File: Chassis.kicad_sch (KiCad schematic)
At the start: 26 parts, among them J1 FR_JST, J10 BL_XT30, J11 Sabre Vertical Header 6, J2 FR_XT30, J3 BR_JST, J4 BR_XT30, J5 IN_JST, J6 IN_XT60, J7 FL_JST, J8 FL_XT30, J9 BL_JST

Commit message: updated xt30 footprints
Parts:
- J10, J2, J4, J8: footprint Robomaster_ICs:AMASS_XT30U-F_1x02_P5.0mm_Vertical -> Connector_AMASS:AMASS_XT30UPB-F_1x02_P5.0mm_Vertical
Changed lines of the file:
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@@
       (effects (font (size 1.27 1.27)))
     )
-    (property "Footprint" "Robomaster_ICs:AMASS_XT30U-F_1x02_P5.0mm_Vertical" (at 130.81 96.52 0)
+    (property "Footprint" "Connector_AMASS:AMASS_XT30UPB-F_1x02_P5.0mm_Vertical" (at 130.81 96.52 0)
       (effects (font (size 1.27 1.27)) hide)
     )
@@
       (effects (font (size 1.27 1.27)))
     )
-    (property "Footprint" "Robomaster_ICs:AMASS_XT30U-F_1x02_P5.0mm_Vertical" (at 130.81 121.92 0)
+    (property "Footprint" "Connector_AMASS:AMASS_XT30UPB-F_1x02_P5.0mm_Vertical" (at 130.81 121.92 0)
       (effects (font (size 1.27 1.27)) hide)
     )
@@
       (effects (font (size 1.27 1.27)))
     )
-    (property "Footprint" "Robomaster_ICs:AMASS_XT30U-F_1x02_P5.0mm_Vertical" (at 130.81 147.32 0)
+    (property "Footprint" "Connector_AMASS:AMASS_XT30UPB-F_1x02_P5.0mm_Vertical" (at 130.81 147.32 0)
       (effects (font (size 1.27 1.27)) hide)
     )
@@
       (effects (font (size 1.27 1.27)))
     )
-    (property "Footprint" "Robomaster_ICs:AMASS_XT30U-F_1x02_P5.0mm_Vertical" (at 130.81 69.85 0)
-      (effects (font (size 1.27 1.27)) hide)
-    )
+    (property "Footprint" "Connector_AMASS:AMASS_XT30UPB-F_1x02_P5.0mm_Vertical" (at 130.81 69.85 0)
+      (effects (font (size 1.27 1.27)) hide)
+    )

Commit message: Add box to schematic
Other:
- note added: "Mounting Holes"
- moved on the sheet: H1, H2, H3, H4, H5, H6, H7, H8, H9

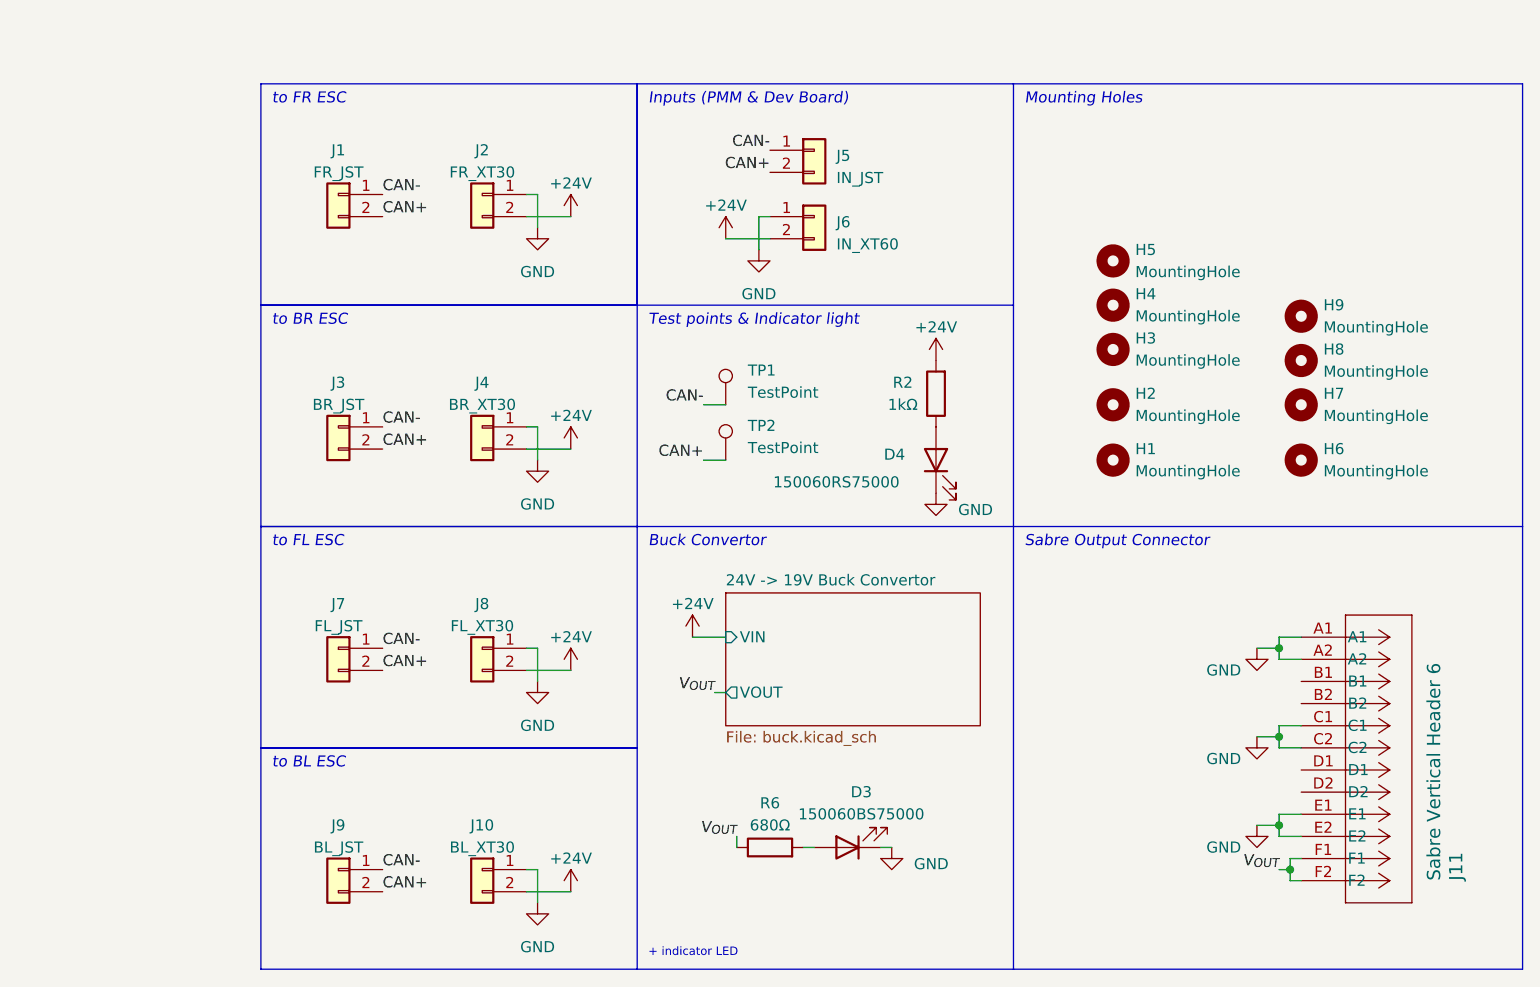
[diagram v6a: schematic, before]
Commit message: +5V buck
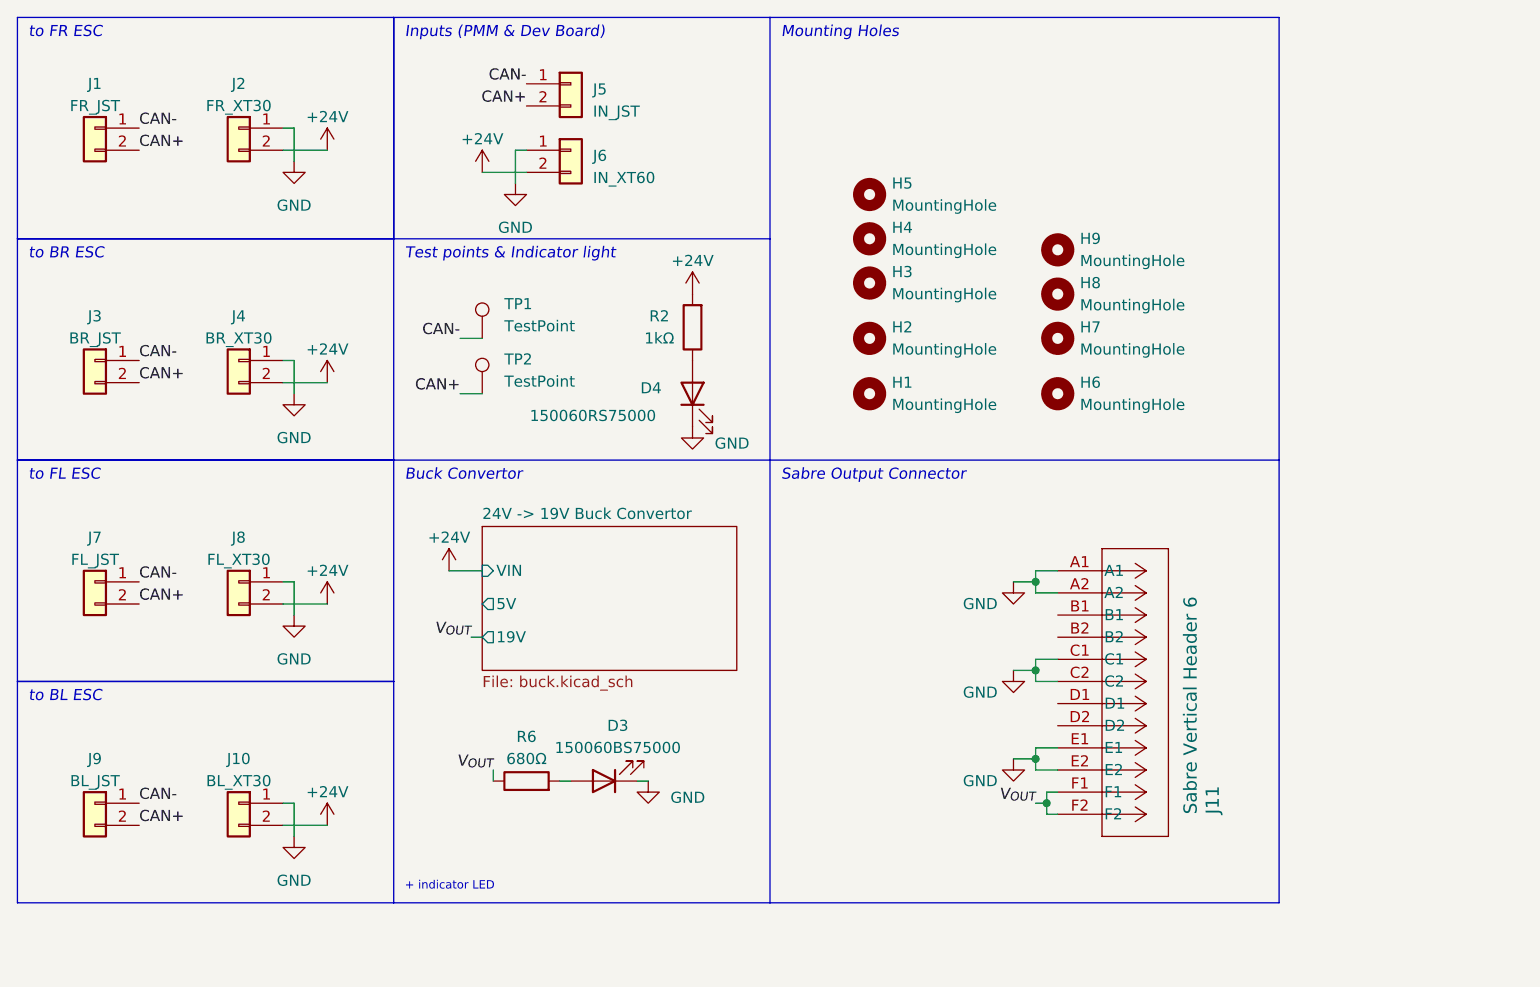
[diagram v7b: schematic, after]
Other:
- sheet 24V -> 19V Buck Convertor ports: added 19V, 5V; removed VOUT
- company: (none) -> UT RoboMasters
- title: (none) -> Chassis
- moved on the sheet: D3, D4, H1, H2, H3, H4, H5, H6, H7, H8, H9, J1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

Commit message: Straightened some kinks
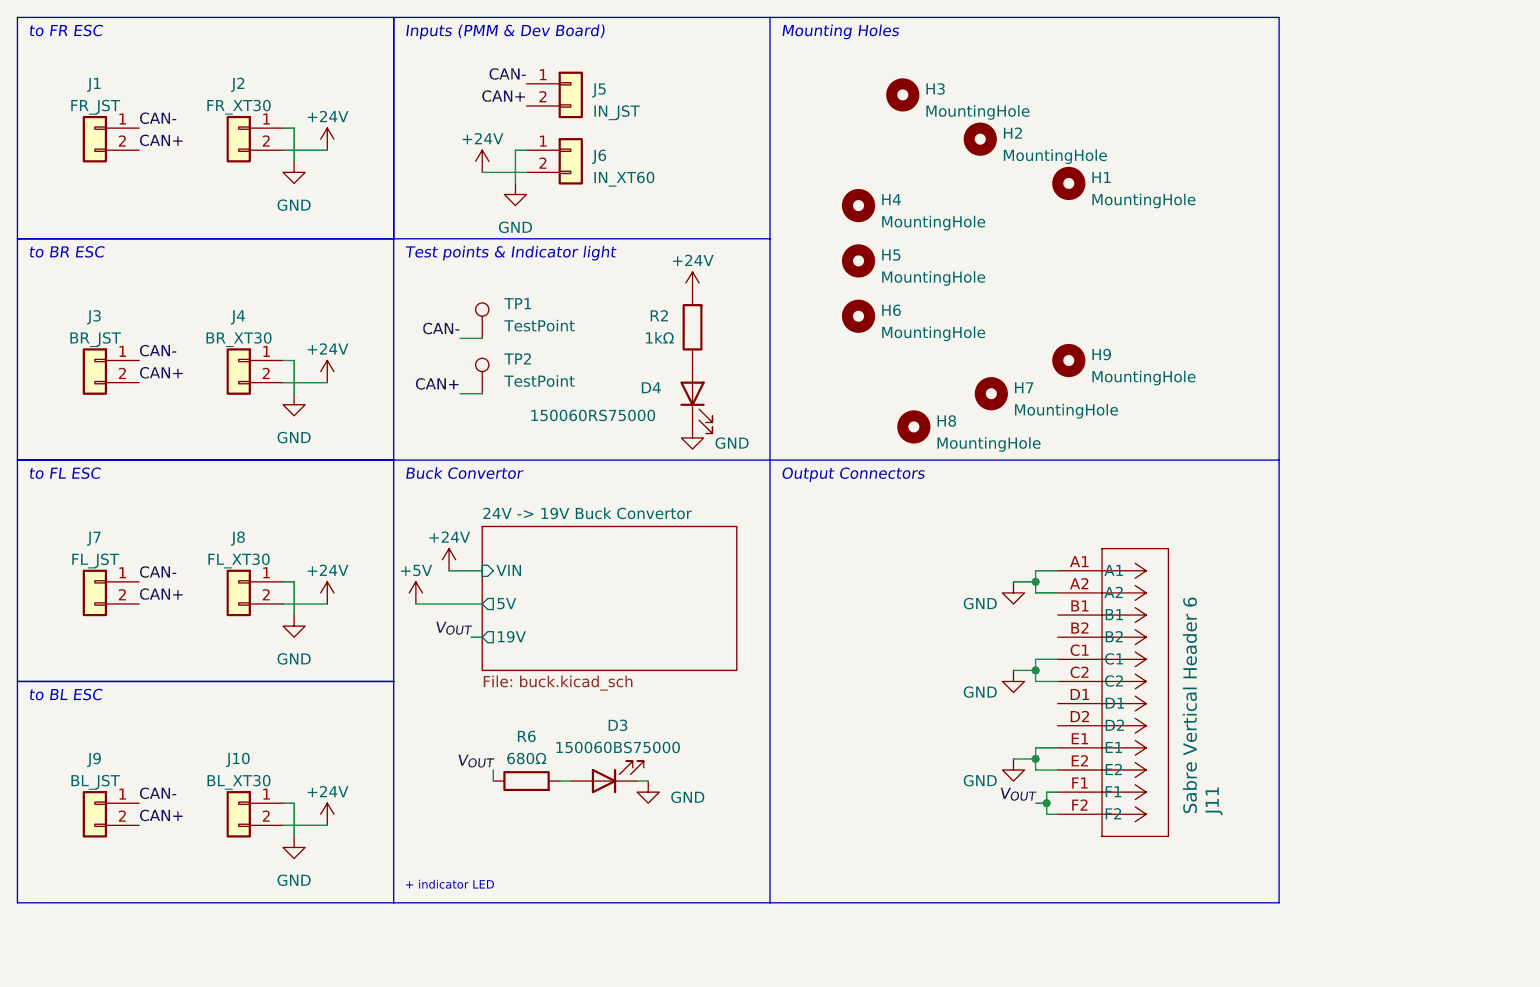
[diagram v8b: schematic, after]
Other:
- note added: "Output Connectors"
- note removed: "Sabre Output Connector"
- moved on the sheet: H1, H2, H3, H4, H5, H6, H7, H8, H9
